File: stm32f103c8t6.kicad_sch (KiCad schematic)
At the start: 1 part, among them U1 STM32F103C8Tx

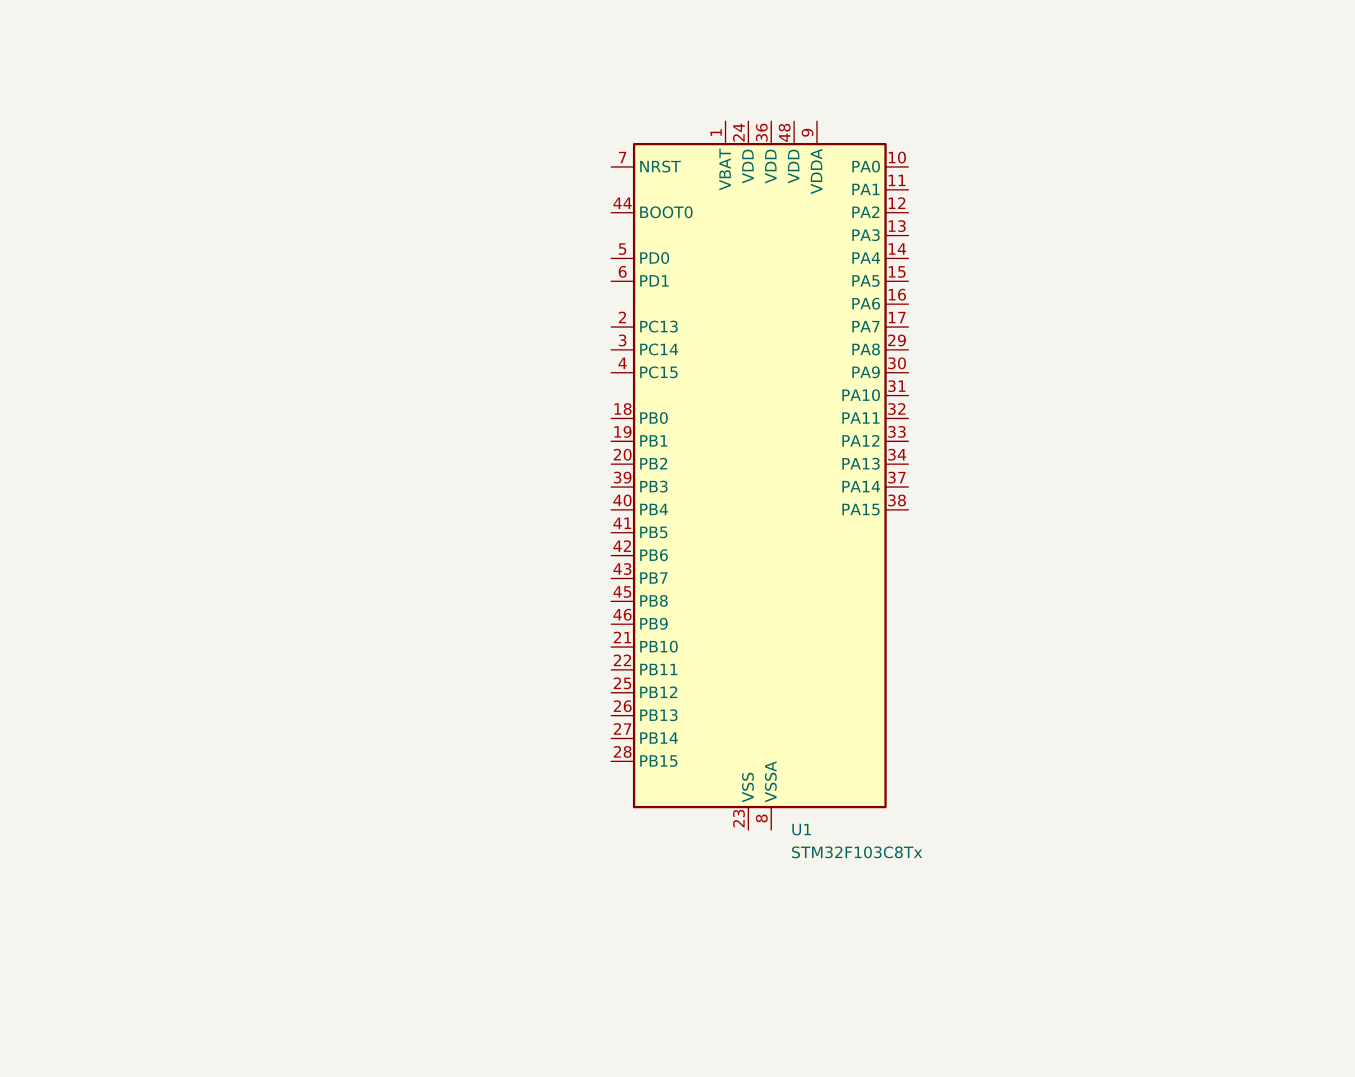
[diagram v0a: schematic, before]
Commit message: Add CPU and Resistor to PCB
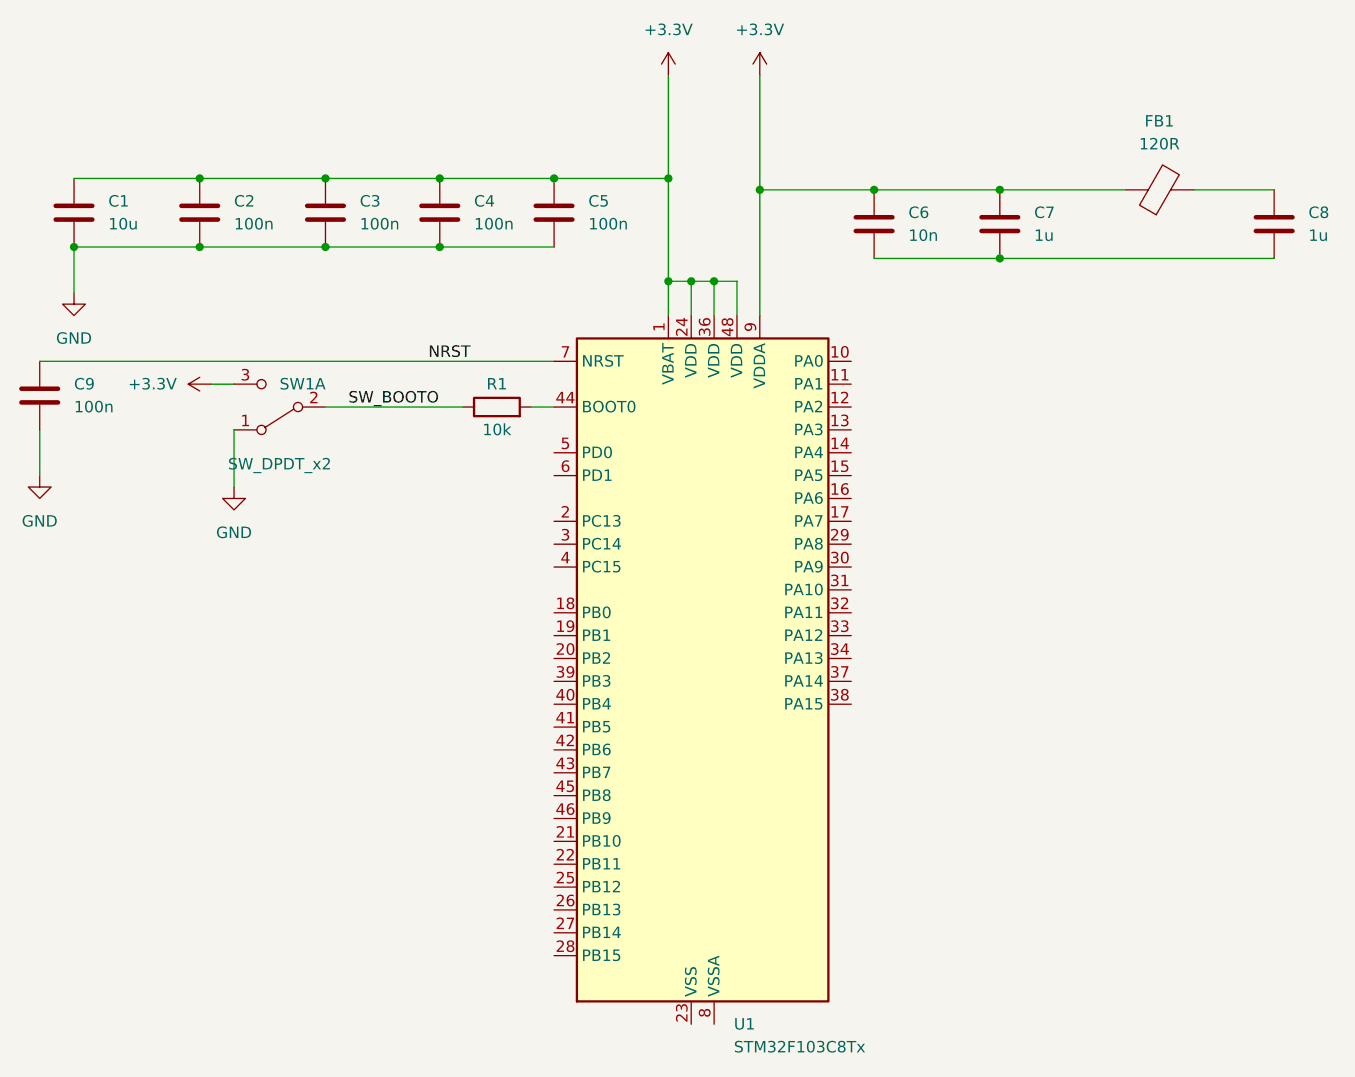
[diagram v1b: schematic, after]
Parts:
- added C1: 10u, Capacitor_Tantalum_SMD:CP_EIA-1608-10_AVX-L, symbol Device:C
- added C2, C3, C4, C5, C9: 100n, Capacitor_Tantalum_SMD:CP_EIA-1608-10_AVX-L, symbol Device:C
- added C6: 10n, Capacitor_Tantalum_SMD:CP_EIA-1608-10_AVX-L, symbol Device:C
- added C7, C8: 1u, Capacitor_Tantalum_SMD:CP_EIA-1608-10_AVX-L, symbol Device:C
- added FB1: 120R, Capacitor_Tantalum_SMD:CP_EIA-1608-10_AVX-L, symbol Device:FerriteBead
- added R1: 10k, Resistor_SMD:R_0603_1608Metric, symbol Device:R
- added SW1: SW_DPDT_x2, symbol Switch:SW_DPDT_x2
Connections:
- net +3.3V: now reaches U1.1 (VBAT)
- net +3.3V: now also U1.24 (VDD), U1.36 (VDD), U1.48 (VDD), U1.9 (VDDA), C1.1, C2.1, C3.1, C4.1, C5.1, C6.1, C7.1, FB1.1, SW1.3 (C)
- net at U1.44 (BOOT0): now also R1.2
- net NRST: now reaches U1.7 (NRST)
- net NRST: now also C9.1
- new net: C8.1, FB1.2
- new net: C6.2, C7.2, C8.2
- new net GND: C1.2, C2.2, C3.2, C4.2, C5.2, C9.2, SW1.1 (A)
- new net SW_BOOTO: R1.1, SW1.2 (B)
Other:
- moved on the sheet: U1

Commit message: PCB Layout
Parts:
- removed SW1: SW_DPDT_x2, symbol Switch:SW_DPDT_x2
- added C1, C2: 22uF, Capacitor_SMD:C_0805_2012Metric, symbol Device:C
- added C12, C13: 10pF, Capacitor_SMD:C_0402_1005Metric, symbol Device:C
- added D1: LED, LED_SMD:LED_0603_1608Metric, symbol Device:LED
- added J1: USB_B_Micro, Connector_USB:USB_Micro-B_Wuerth_629105150521, symbol Connector:USB_B_Micro
- added J2, J3, J4: Conn_01x04_Pin, Connector_PinHeader_2.54mm:PinHeader_1x04_P2.54mm_Vertical, symbol Connector:Conn_01x04_Pin
- added R1, R4, R5: 1k5, Resistor_SMD:R_0402_1005Metric, symbol Device:R
- added R3: 1K5, Resistor_SMD:R_0402_1005Metric, symbol Device:R
- added SW1: SW_SPDT, Button_Switch_THT:SW_E-Switch_EG1224_SPDT_Angled, symbol Switch:SW_SPDT
- added U1: AMS1117-3.3, Package_TO_SOT_SMD:SOT-223-3_TabPin2, symbol Regulator_Linear:AMS1117-3.3
- added Y1: 16Mhz, Crystal:Crystal_SMD_3225-4Pin_3.2x2.5mm, symbol Device:Crystal_GND24
- C10: renamed from C8; footprint Capacitor_Tantalum_SMD:CP_EIA-1608-10_AVX-L -> Capacitor_SMD:C_0402_1005Metric
- C11: renamed from C9; footprint Capacitor_Tantalum_SMD:CP_EIA-1608-10_AVX-L -> Capacitor_SMD:C_0402_1005Metric
- C3: renamed from C1; footprint Capacitor_Tantalum_SMD:CP_EIA-1608-10_AVX-L -> Capacitor_SMD:C_0805_2012Metric
- C4: renamed from C2; footprint Capacitor_Tantalum_SMD:CP_EIA-1608-10_AVX-L -> Capacitor_SMD:C_0402_1005Metric
- C5: renamed from C3; footprint Capacitor_Tantalum_SMD:CP_EIA-1608-10_AVX-L -> Capacitor_SMD:C_0402_1005Metric
- C6: renamed from C4; footprint Capacitor_Tantalum_SMD:CP_EIA-1608-10_AVX-L -> Capacitor_SMD:C_0402_1005Metric
- C7: renamed from C5; footprint Capacitor_Tantalum_SMD:CP_EIA-1608-10_AVX-L -> Capacitor_SMD:C_0402_1005Metric
- C8: renamed from C6; footprint Capacitor_Tantalum_SMD:CP_EIA-1608-10_AVX-L -> Capacitor_SMD:C_0402_1005Metric
- C9: renamed from C7; footprint Capacitor_Tantalum_SMD:CP_EIA-1608-10_AVX-L -> Capacitor_SMD:C_0402_1005Metric
- FB1: footprint Capacitor_Tantalum_SMD:CP_EIA-1608-10_AVX-L -> Inductor_SMD:L_0603_1608Metric
- R2: renamed from R1; footprint Resistor_SMD:R_0603_1608Metric -> Resistor_SMD:R_0402_1005Metric
- renumbered U1 to U2
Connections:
- net +3.3V: now also C2.1, D1.2 (A), J3.1 (Pin_1), R3.1, SW1.1 (A), U1.2 (VO)
- net GND: now also U2.23 (VSS), U2.35 (VSS), U2.47 (VSS), U2.8 (VSSA), C1.2, C12.2, C13.2, C2.2, J1.5 (GND), J2.4 (Pin_4), J3.4 (Pin_4), J4.4 (Pin_4), R1.2, SW1.3 (C), U1.1 (GND), Y1.2, Y1.4
- net SW_BOOTO: now also SW1.2 (B)
- net I2C2_SCL: now reaches U2.21 (PB10)
- net I2C2_SCL: now also J4.2 (Pin_2), R4.1
- net I2C2_SDA: now reaches U2.22 (PB11)
- net I2C2_SDA: now also J4.3 (Pin_3), R5.1
- net USB_D-: now reaches U2.32 (PA11)
- net USB_D-: now also J1.2 (D-)
- net USB_D+: now reaches U2.33 (PA12)
- net USB_D+: now also J1.3 (D+), R3.2
- net SWDIO: now reaches U2.34 (PA13)
- net SWDIO: now also J3.2 (Pin_2)
- net SWCLK: now reaches U2.37 (PA14)
- net SWCLK: now also J3.3 (Pin_3)
- net USART1_TX: now reaches U2.42 (PB6)
- net USART1_TX: now also J2.2 (Pin_2)
- net USART1_RX: now reaches U2.43 (PB7)
- net USART1_RX: now also J2.3 (Pin_3)
- net HSE_IN: now reaches U2.5 (PD0)
- net HSE_IN: now also C12.1, Y1.1
- net HSE_OUT: now reaches U2.6 (PD1)
- net HSE_OUT: now also C13.1, Y1.3
- new net: D1.1 (K), R1.1
- new net +3V3: J2.1 (Pin_1), J4.1 (Pin_1), R4.2, R5.2
- new net VBUS: C1.1, J1.1 (VBUS), U1.3 (VI)
- no-connect marks 0 -> 29
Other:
- note added: "1x 100nF per VDD pin"
- note added: "CL = 2*(CL0-Cs) = 2*(10-5)pF = 10pF"
- note added: "Microcontroller (and USB)"
- note added: "Pin-out using STM32CubeIDE"
- note added: "Power_Supply"
- note added: "USB App note AN4879"
- note added: "Udemy STM32 Demo PCB"
- note added: "VBUS from USB connector (nom +5V) Min 22uF inp./outp. caps"
- note added: "VDDA Filttering"
- company: (none) -> VNPT Technology
- title: (none) -> Udemy STM32 Demo PCB
- moved on the sheet: C10, C11, C3, C4, C5, C6, C7, C8, C9, FB1, R2, U2

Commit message: Layouting don't compleate
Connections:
- net +3V3 is gone; now on net +3.3V: J2.1 (Pin_1), J4.1 (Pin_1), R4.2, R5.2
